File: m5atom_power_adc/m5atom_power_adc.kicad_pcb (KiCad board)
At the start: 2 copper layers, 80 x 82.5 mm, 133 parts, among them J101 USB_C_Receptacle_USB2.0_16P, J102 Conn_01x04_Pin, J103 SubBatt, J104 MainBatt, J105 I2C, J106 Shunt, J201 Relay0, J202 R0SW, J301 Relay1, J302 R1SW, J401 Relay2, J402 R2SW, J501 GROVE-CONNECTOR, J601 GROVE-CONNECTOR, Q101 AO3401A, Q102 MMBT2222A, Q103 AO3401A, Q201 MMBT2222A, Q301 MMBT2222A, Q401 MMBT2222A, Q501 AO3401A, Q502 MMBT2222A, Q601 AO3401A, Q602 MMBT2222A, SW101 Boot, SW102 Reset, SW103 Btn0, SW104 Btn1, U101 LM2596S-5, U102 AMS1117-3.3, U103 ESP32-S3-MINI-1, U104 AMS1117-3.3, U105 LTC2944, U106 ADS1115IDGS

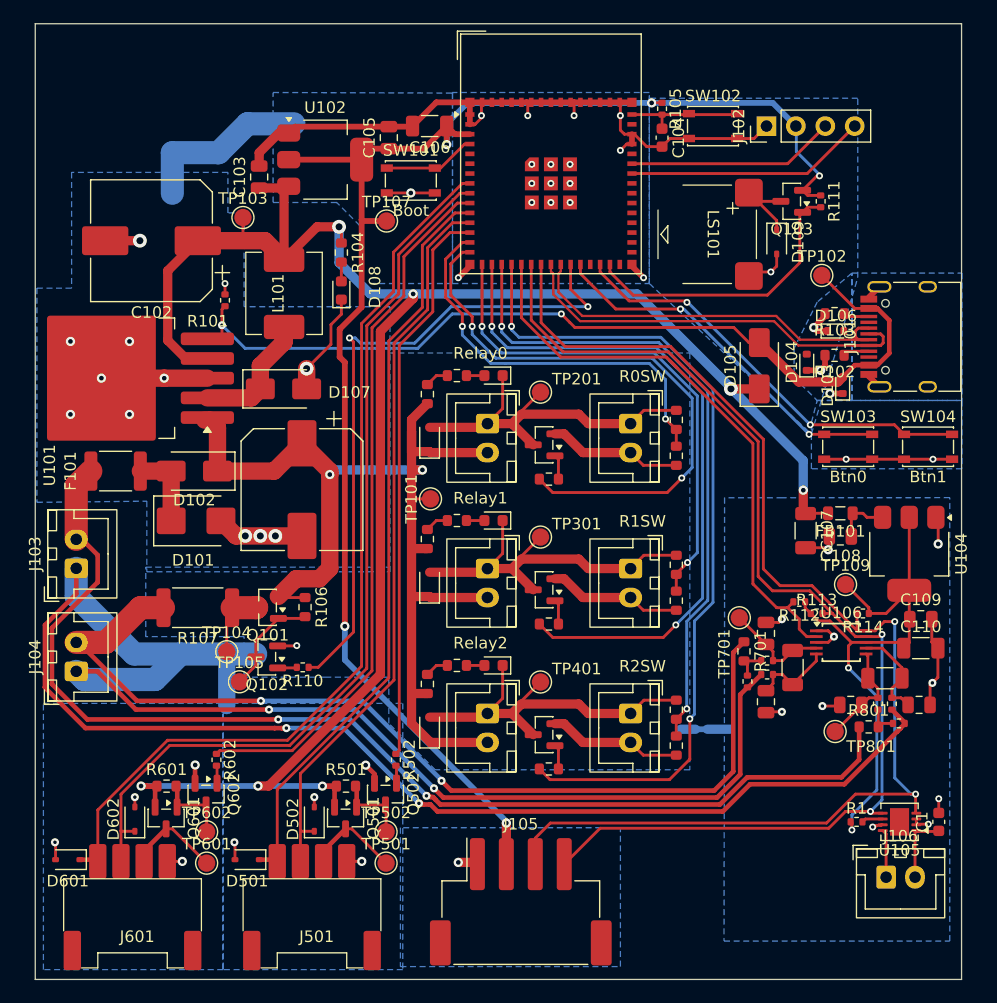
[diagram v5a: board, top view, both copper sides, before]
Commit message: chore: PCBネジ穴追加・シルク整理・ロゴ追加・フットプリント修正
- ネジ穴を追加
- シルク文字・ロゴを整理・追加（k_icon フットプリント）
- HY2.0-4PZZ コネクタフットプリントを追加
- 各サブシートのフットプリント修正
- production/ を .gitignore に追加

Co-Authored-By: Claude Sonnet 4.6 <noreply@anthropic.com>
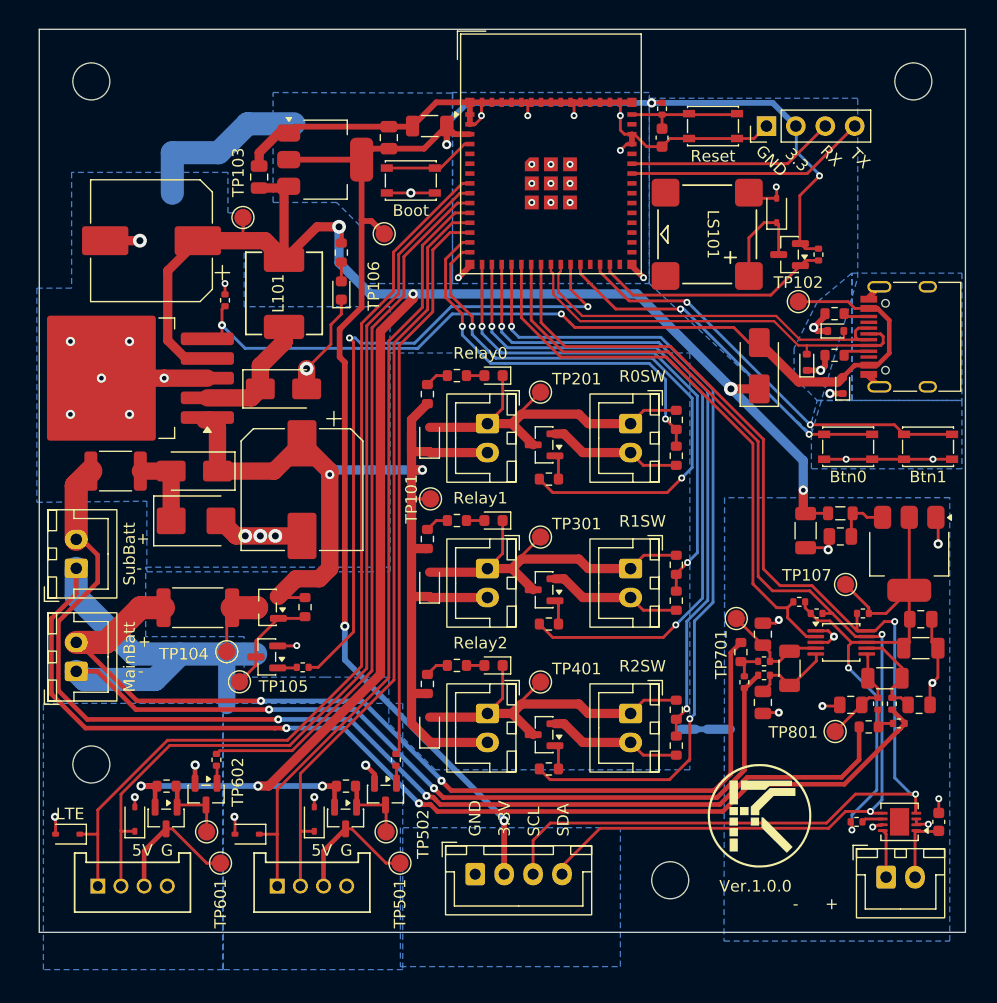
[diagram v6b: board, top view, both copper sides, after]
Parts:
- added G***: LOGO, 000_Local:k_icon, F.Cu at (123.5, 104.0)
- added REF**: MountingHole_3.2mm_M3_ISO7380, MountingHole:MountingHole_3.2mm_M3_ISO7380, F.Cu at (115.8, 109.5)
- added REF**: MountingHole_3.2mm_M3_ISO7380, MountingHole:MountingHole_3.2mm_M3_ISO7380, F.Cu at (136.8, 40.5)
- added REF**: MountingHole_3.2mm_M3_ISO7380, MountingHole:MountingHole_3.2mm_M3_ISO7380, F.Cu at (65.8, 40.5)
- added REF**: MountingHole_3.2mm_M3_ISO7380, MountingHole:MountingHole_3.2mm_M3_ISO7380, F.Cu at (65.8, 99.5)
- J105: footprint Connector_JST:JST_XH_S4B-XH-SM4-TB_1x04-1MP_P2.50mm_Horizontal -> Connector_JST:JST_XH_B4B-XH-A_1x04_P2.50mm_Vertical
- J501, J601: footprint 000_Local:HY2.0-4PWB -> 000_Local:HY2.0-4PZZ
- U106: footprint Package_SO:TSSOP-10_3x3mm_P0.5mm -> Package_SO:VSSOP-10_3x3mm_P0.5mm
- moved J105 4.61 mm to (99.0, 109.0)
- moved R109 4.60 mm to (128.6, 55.5)
- moved Q103 4.60 mm to (126.1, 55.5)
- moved J501 3.87 mm to (84.9, 110.0), turned to 180 degrees
- moved J601 3.87 mm to (69.4, 110.0), turned to 180 degrees
- moved TP102 3.04 mm to (126.9, 59.6)
- moved D109 2.71 mm to (125.0, 51.7), turned to 90 degrees
- moved D501 2.20 mm to (79.3, 105.6)
- moved D601 2.20 mm to (63.8, 105.6)
- moved TP501 1.20 mm to (92.5, 108.1)
- moved TP601 1.20 mm to (77.0, 108.1)
- moved TP106 1.12 mm to (91.1, 53.7)
- moved R703 0.27 mm to (123.9, 90.6)
- moved C701 0.27 mm to (123.8, 94.2)
- moved C702 0.27 mm to (123.8, 88.3)
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- renumbered C1 to C111, NT102 to NT101, NT101 to NT102, NT104 to NT103, R110 to R108, R111 to R109, R1 to R110, R112 to R111, R113 to R112, R114 to R113, TP107 to TP106, TP109 to TP107
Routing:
- net +3.3V: track 132.6 -> 138.2 mm
- net SPEAKER: track 25.2 -> 20.7 mm
- net GND1: track 90.7 -> 86.3 mm, vias 22 -> 19
- net Net-(Q601-D): track 8.33 -> 11.7 mm
- net Net-(Q501-D): track 8.33 -> 11.7 mm
- net /GU_1: track 63.3 -> 65.5 mm
- net /LTE_TX: track 78.0 -> 80.1 mm
- net /LTE_RX: track 79.9 -> 82.0 mm
- net /GU_0: track 65.3 -> 67.3 mm
- net VBUS: track 76.5 -> 77.6 mm
- net GND2: track 100.2 -> 101.2 mm
- net Net-(D109-K): track 8.12 -> 9.07 mm
- net /SDA: track 99.4 -> 100.3 mm
- net /SCL: track 110.0 -> 111.0 mm
- net USB_D+: track 34.2 -> 35.0 mm
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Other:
- board size 80 x 82.5 mm -> 80 x 78 mm
- board text added: "+"
- board text added: "-"
- board text added: "3.3"
- board text added: "3.3V"
- board text added: "5V"
- board text added: "G"
- board text added: "GND"
- board text added: "LTE"
- board text added: "RX"
- board text added: "SCL"
- board text added: "SDA"
- board text added: "TX"
- board text added: "Ver.1.0.0"

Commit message: feat: GroveUnitに電源インジケーターLED追加・PCB配置
回路図：電源インジケーターLED（LED+抵抗）を追加
PCB：LED・抵抗のフットプリント配置・配線
CLAUDE.md：KiCadファイル直接編集禁止ルールを追記

Co-Authored-By: Claude Sonnet 4.6 <noreply@anthropic.com>
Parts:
- added D503: LED, LED_SMD:LED_0603_1608Metric, F.Cu at (91.8, 110.2)
- added D603: LED, LED_SMD:LED_0603_1608Metric, F.Cu at (76.3, 110.2)
- added R503: 200, Resistor_SMD:R_0603_1608Metric, F.Cu at (91.8, 111.9)
- added R603: 200, Resistor_SMD:R_0603_1608Metric, F.Cu at (76.3, 111.9)
- moved TP501 0.35 mm to (92.6, 107.7)
- moved TP601 0.35 mm to (77.1, 107.7)
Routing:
- net Net-(D503-A): track 11.7 -> 14.4 mm
- net Net-(D603-A): track 11.7 -> 14.3 mm
- net GND1: track 86.3 -> 88.7 mm, vias 19 -> 21
- net Net-(D503-K): track 0.00 -> 1.80 mm
- net Net-(D603-K): track 0.00 -> 1.71 mm

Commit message: chore: KiCadプロジェクト更新（回路図・PCBレイアウト各種修正）
Co-Authored-By: Claude Sonnet 4.6 <noreply@anthropic.com>
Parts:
- removed C111: 1uF X7R, Capacitor_SMD:C_0603_1608Metric
- removed R110: 10k, Resistor_SMD:R_0402_1005Metric
- removed U105: LTC2944, Package_DFN_QFN:DFN-8-1EP_3x3mm_P0.5mm_EP1.65x2.38mm
- added C112: 100nF, Capacitor_SMD:C_0603_1608Metric, F.Cu at (131.4, 104.6)
- added C501: 47uF, Capacitor_SMD:C_1206_3216Metric, F.Cu at (91.4, 99.7)
- added C502: 100nF, Capacitor_SMD:C_0603_1608Metric, F.Cu at (87.4, 100.3)
- added C601: 47uF, Capacitor_SMD:C_1206_3216Metric, F.Cu at (76.3, 99.6)
- added C602: 100nF, Capacitor_SMD:C_0603_1608Metric, F.Cu at (72.4, 100.4)
- added U108: INA228, Package_SO:VSSOP-10_3x3mm_P0.5mm, F.Cu at (135.7, 104.2)
- moved TP602 4.48 mm to (79.7, 103.2)
- moved R603 3.24 mm to (77.1, 102.3), turned to 180 degrees
- moved R503 3.04 mm to (92.6, 102.1), turned to 180 degrees
- moved TP502 3.04 mm to (94.1, 106.4)
- moved Q602 2.74 mm to (75.7, 104.8)
- moved Q502 2.54 mm to (91.2, 104.6)
- moved D503 1.66 mm to (84.0, 105.5), turned to 0 degrees
- moved D603 1.66 mm to (68.5, 105.5), turned to 0 degrees
- moved TP601 1.26 mm to (75.9, 108.1)
- moved TP501 1.20 mm to (91.4, 107.8)
- moved Q601 0.74 mm to (72.2, 104.9)
- moved R602 0.74 mm to (72.2, 102.1)
- moved Q501 0.60 mm to (87.4, 104.6)
- moved R502 0.60 mm to (87.4, 101.9)
- renumbered D503 to D501, D501 to D502, D502 to D503, D603 to D601, D601 to D602, D602 to D603, R503 to R501, R501 to R502, R502 to R503, R603 to R601, R601 to R602, R602 to R603
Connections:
- net Btn0 renamed /Btn0
- net Btn1 renamed /Btn1
- net CHG_ON renamed /CHG_ON
- net RXD0 renamed /RXD0
- net SPEAKER renamed /SPEAKER
- net TXD0 renamed /TXD0
- net USB_D+ renamed /USB_D+
- net USB_D- renamed /USB_D-
- U103 pad 31: unconnected-(U103-IO35-Pad31) -> /INA_ALERT
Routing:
- net /INA_ALERT: track 0.00 -> 66.2 mm, vias 0 -> 2
- net GND1: track 88.7 -> 102.8 mm, vias 21 -> 37
- net +5V: track 170.7 -> 181.5 mm
- net SENSE+: track 6.06 -> 12.9 mm
- net Net-(Q601-G): track 6.74 -> 12.7 mm
- net /SDA: track 100.3 -> 105.9 mm
- net /GU_EN: track 48.7 -> 53.0 mm
- net SENSE-: track 4.14 -> 6.26 mm
- net Net-(D601-A): track 14.3 -> 12.2 mm
- net Net-(Q501-G): track 6.74 -> 8.68 mm
- net Net-(D501-A): track 14.4 -> 12.5 mm
- net Net-(U105-~ALCC): track 1.86 -> 0.00 mm
- net /SCL: track 111.0 -> 109.6 mm
- net +3.3VA: track 48.6 -> 47.5 mm
- net /LTE_EN: track 60.9 -> 61.8 mm
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- added copper zone on F.Cu, net GND1
- added copper zone on F.Cu, net GND2
- added copper zone on F.Cu, net GNDA
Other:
- board text removed: "3.3"
